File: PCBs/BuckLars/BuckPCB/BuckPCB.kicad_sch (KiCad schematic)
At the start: 8 parts, among them J1 Program_header, SW1 RESET, SW2 Boot, U1 ESP32-WROOM-32D

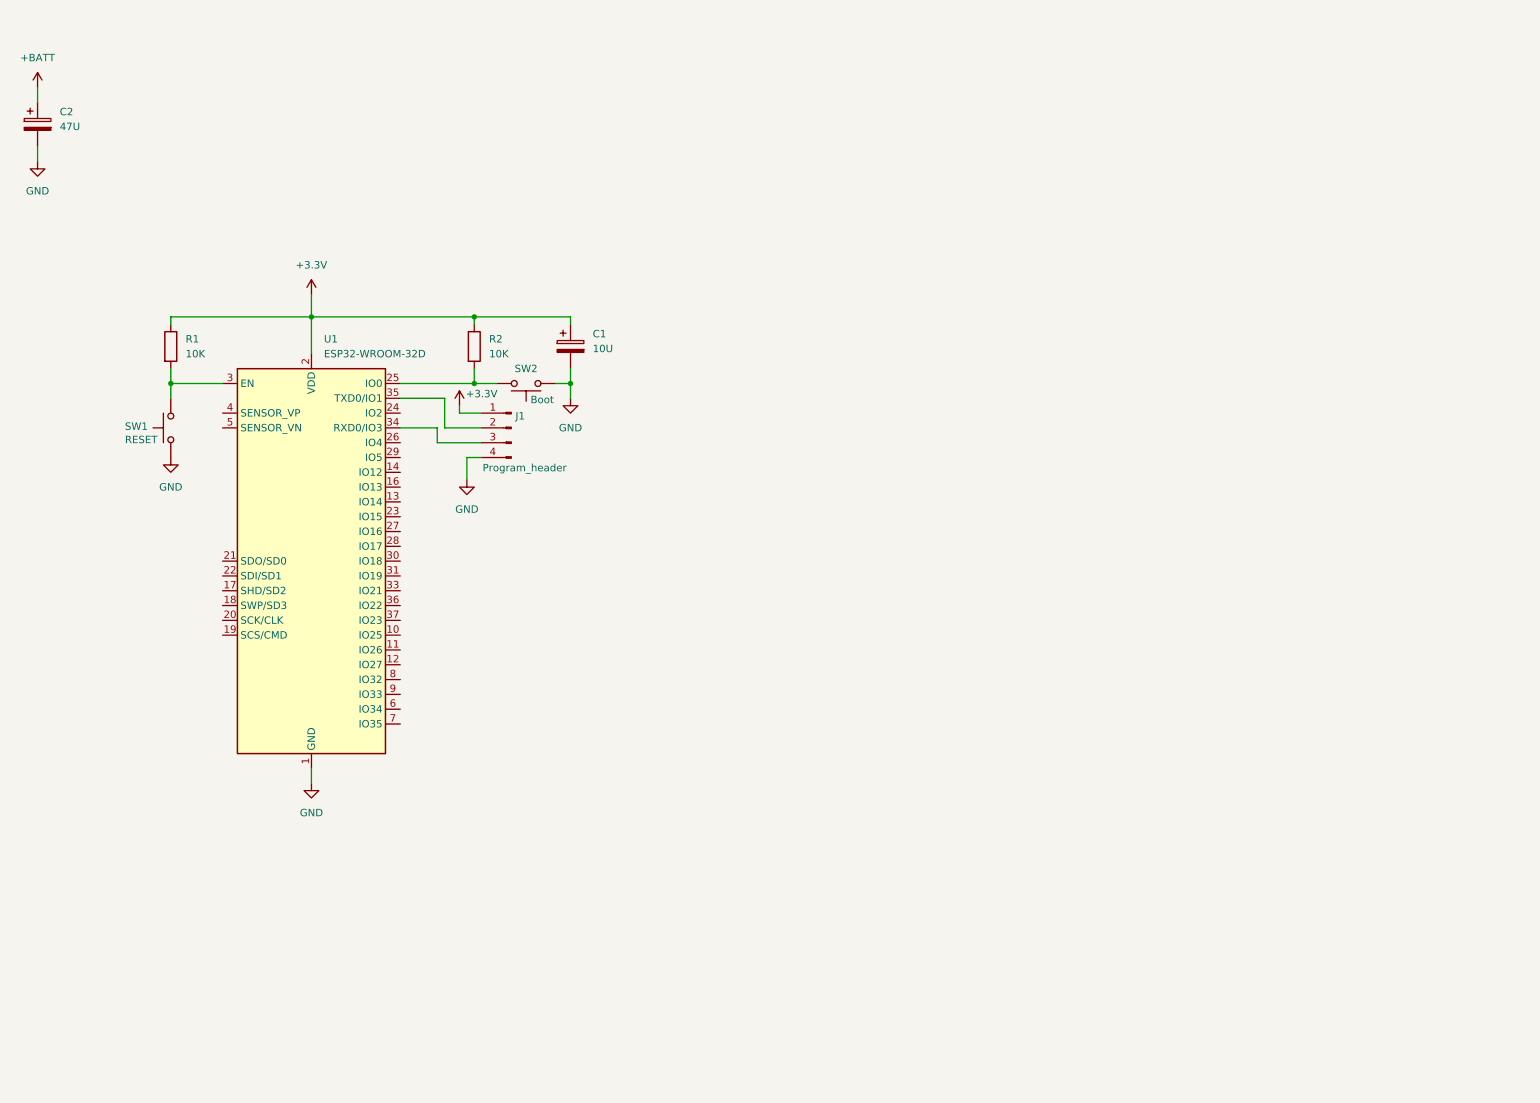
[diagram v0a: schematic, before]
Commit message: added buck converter to schematic
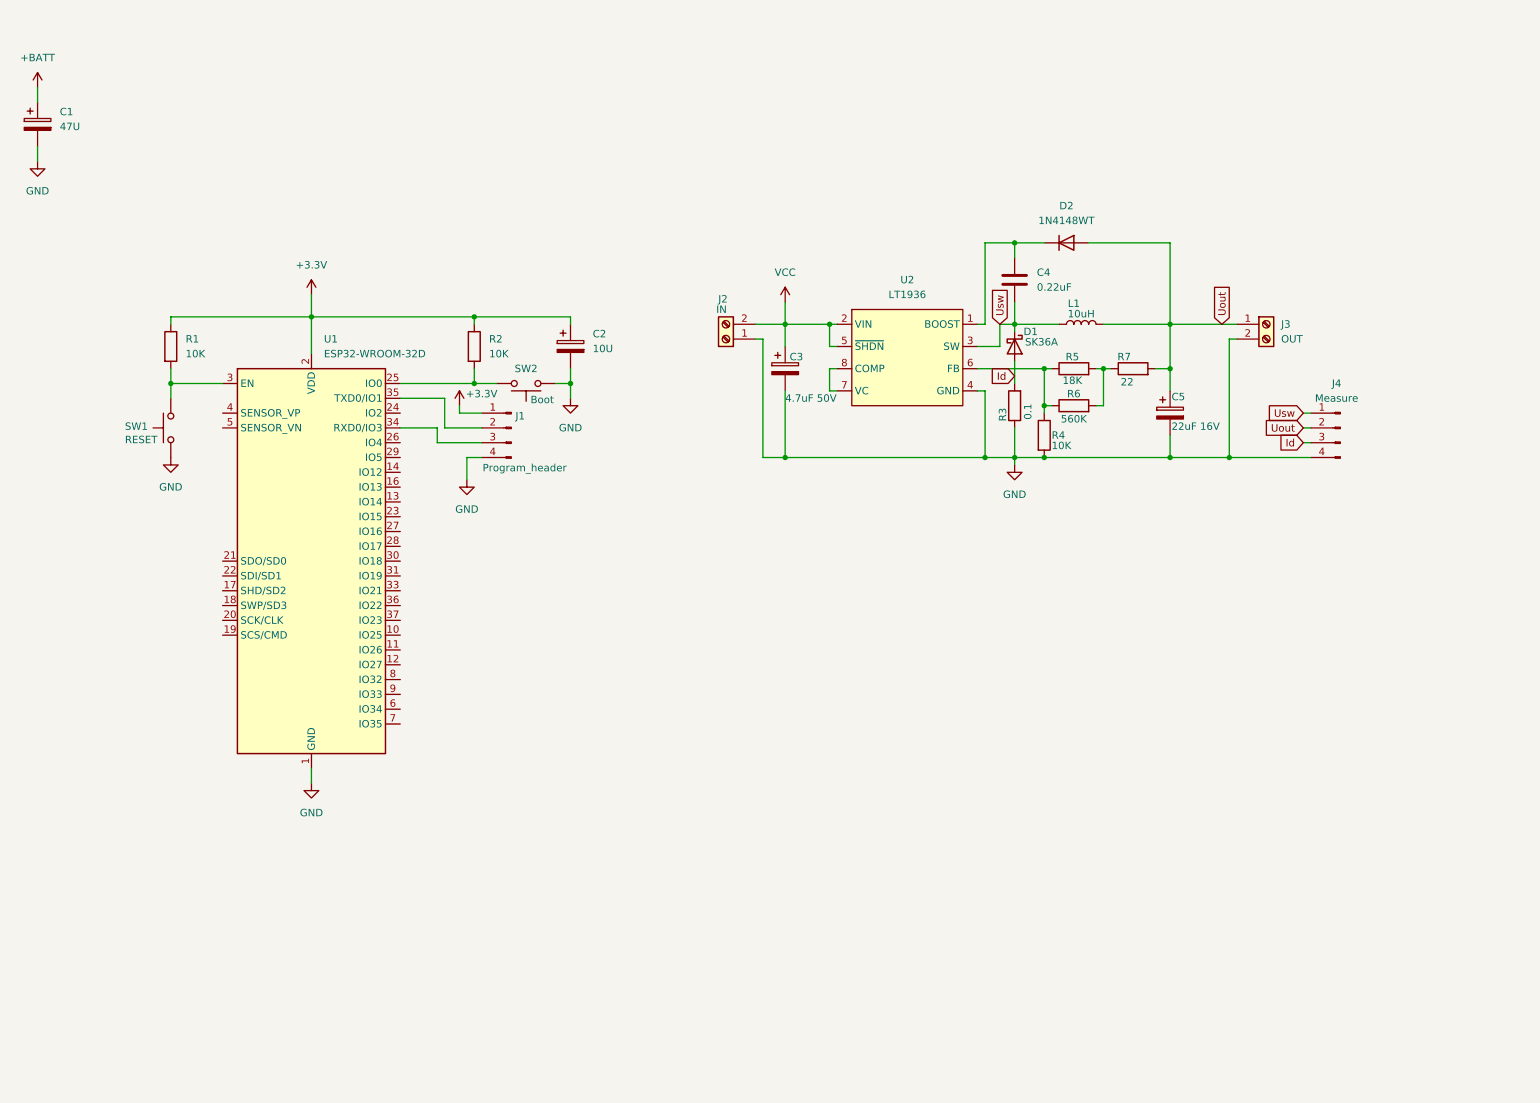
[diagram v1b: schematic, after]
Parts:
- added C3: 4.7uF 50V, Capacitor_SMD:CP_Elec_4x5.4, symbol Device:C_Polarized
- added C4: 0.22uF, Capacitor_SMD:C_1206_3216Metric_Pad1.33x1.80mm_HandSolder, symbol Device:C
- added C5: 22uF 16V, Capacitor_Tantalum_SMD:CP_EIA-3528-12_Kemet-T_HandSolder, symbol Device:C_Polarized
- added D1: SK36A, Diode_SMD:D_SMC, symbol Device:D_Schottky
- added D2: 1N4148WT, Diode_SMD:D_SOD-523, symbol Diode:1N4148WT
- added J2: IN, TerminalBlock:TerminalBlock_MaiXu_MX126-5.0-02P_1x02_P5.00mm, symbol Connector:Screw_Terminal_01x02
- added J3: OUT, TerminalBlock:TerminalBlock_MaiXu_MX126-5.0-02P_1x02_P5.00mm, symbol Connector:Screw_Terminal_01x02
- added J4: Measure, Connector_PinHeader_2.54mm:PinHeader_1x04_P2.54mm_Vertical, symbol Connector:Conn_01x04_Pin
- added L1: 10uH, Inductor_SMD:L_7.3x7.3_H4.5, symbol Device:L
- added R3: 0.1, Resistor_SMD:R_1206_3216Metric_Pad1.30x1.75mm_HandSolder, symbol Device:R
- added R4: 10K, Resistor_SMD:R_1206_3216Metric_Pad1.30x1.75mm_HandSolder, symbol Device:R
- added R5: 18K, Resistor_SMD:R_1206_3216Metric_Pad1.30x1.75mm_HandSolder, symbol Device:R
- added R6: 560K, Resistor_SMD:R_1206_3216Metric_Pad1.30x1.75mm_HandSolder, symbol Device:R
- added R7: 22, Resistor_SMD:R_1206_3216Metric_Pad1.30x1.75mm_HandSolder, symbol Device:R
- added U2: LT1936, Package_SO:MSOP-8-1EP_3x3mm_P0.65mm_EP1.95x2.15mm, symbol New_Library:LT1936
- renumbered C2 to C1, C1 to C2
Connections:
- net GND: now also C3.2, C5.2, J2.1 (Pin_1), J3.2 (Pin_2), J4.4 (Pin_4), R3.1, R4.2, U2.4 (GND)
- new net: R4.1, R5.1, R6.1, U2.6 (FB)
- new net: R5.2, R6.2, R7.1
- new net: C4.1, D2.1 (K), U2.1 (BOOST)
- new net: U2.7 (VC), U2.8 (COMP)
- new net Id: D1.2 (A), J4.3 (Pin_3), R3.2
- new net Uout: C5.1, D2.2 (A), J3.1 (Pin_1), J4.2 (Pin_2), L1.2, R7.2
- new net Usw: C4.2, D1.1 (K), J4.1 (Pin_1), L1.1, U2.3 (SW)
- new net VCC: C3.1, J2.2 (Pin_2), U2.2 (VIN), U2.5 (~{SHDN})

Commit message: cleanup chematic and assinged footprints
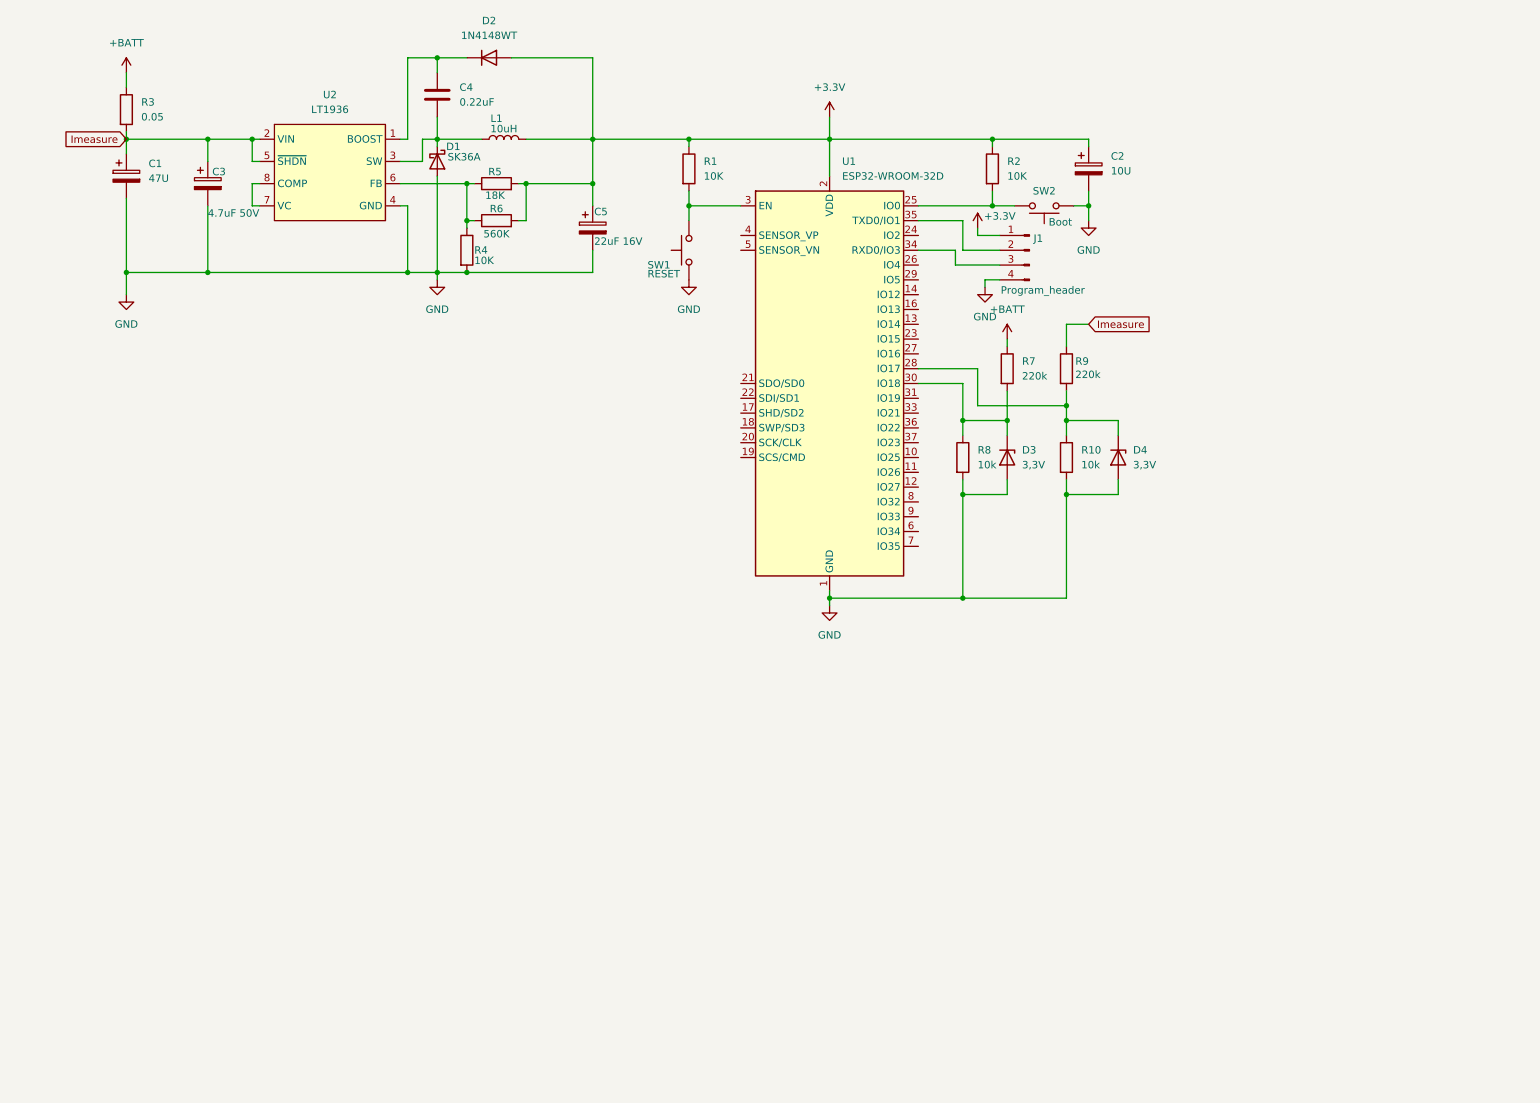
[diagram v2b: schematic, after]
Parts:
- removed J2: IN, TerminalBlock:TerminalBlock_MaiXu_MX126-5.0-02P_1x02_P5.00mm, symbol Connector:Screw_Terminal_01x02
- removed J3: OUT, TerminalBlock:TerminalBlock_MaiXu_MX126-5.0-02P_1x02_P5.00mm, symbol Connector:Screw_Terminal_01x02
- removed J4: Measure, Connector_PinHeader_2.54mm:PinHeader_1x04_P2.54mm_Vertical, symbol Connector:Conn_01x04_Pin
- added D3, D4: 3,3V, Diode_SMD:D_1206_3216Metric, symbol Device:D_Zener
- added R10, R8: 10k, Resistor_SMD:R_1206_3216Metric_Pad1.30x1.75mm_HandSolder, symbol Device:R
- added R9: 220k, Resistor_SMD:R_1206_3216Metric_Pad1.30x1.75mm_HandSolder, symbol Device:R
- C1, C2: footprint (none) -> Capacitor_SMD:CP_Elec_4x5.3
- J1: footprint (none) -> Connector_PinHeader_2.54mm:PinHeader_1x04_P2.54mm_Vertical
- R1, R2: footprint (none) -> Resistor_SMD:R_1206_3216Metric_Pad1.30x1.75mm_HandSolder
- R3: value 0.1 -> 0.05; footprint Resistor_SMD:R_1206_3216Metric_Pad1.30x1.75mm_HandSolder -> Resistor_SMD:R_4020_10251Metric_Pad1.65x5.30mm_HandSolder
- R7: value 22 -> 220k
- SW1, SW2: footprint (none) -> Button_Switch_SMD:SW_SPST_CK_RS282G05A3
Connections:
- net VCC is gone; now on net Imeasure: C3.1, U2.2 (VIN), U2.5 (~{SHDN})
- net +3.3V: now also C5.1, D2.2 (A), L1.2, R5.2, R6.2
- net +BATT: now also R3.1, R7.1; no longer C1.1
- net GND: now also D1.2 (A), D3.2 (A), D4.2 (A), R10.2, R8.2; no longer R3.1
- net at U1.28 (IO17): now also D4.1 (K), R10.1, R9.2
- net at U1.30 (IO18): now also R7.2, D3.1 (K), R8.1
- net Id renamed Imeasure
- net Imeasure: now also C1.1, R9.1; no longer D1.2 (A)
- removed net Uout: C5.1, D2.2 (A), L1.2, R7.2
- net Usw: no longer names the net of C4.2, D1.1 (K), L1.1, U2.3 (SW)
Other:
- moved on the sheet: C1, C2, C3, C4, C5, D1, D2, J1, L1, R1, R2, R4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

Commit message: added buck converters schematic
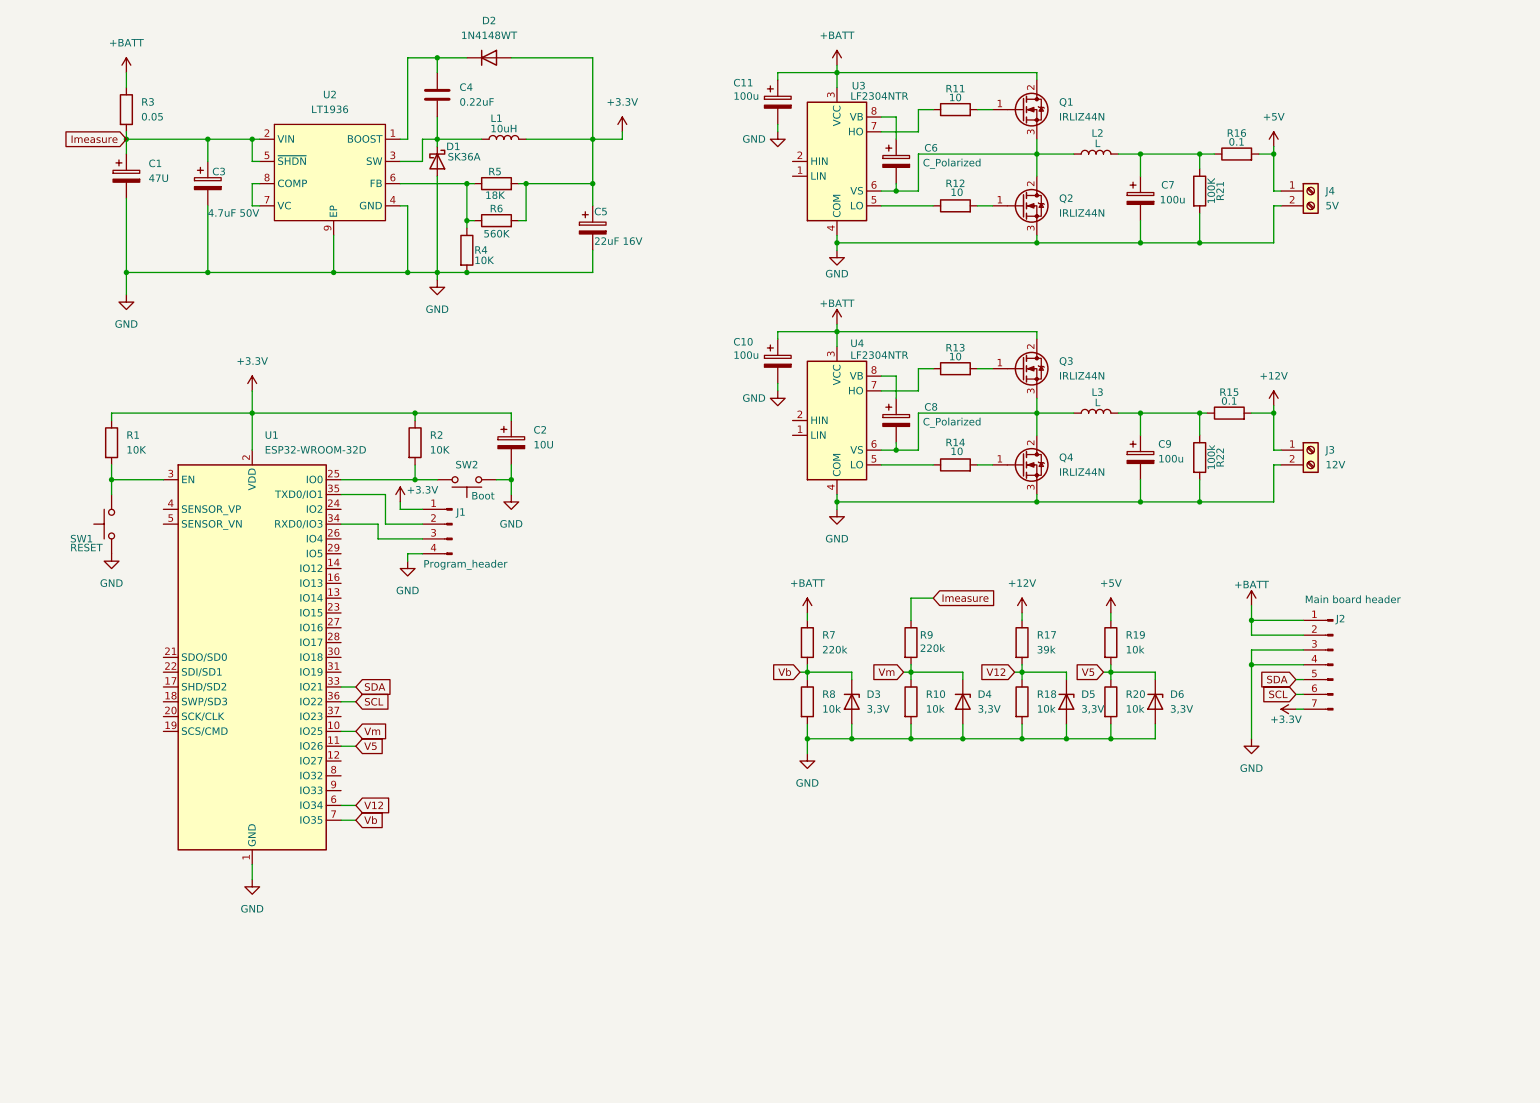
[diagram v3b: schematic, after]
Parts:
- added C10, C11, C7, C9: 100u, Capacitor_SMD:CP_Elec_8x10.5, symbol Device:C_Polarized
- added C6, C8: C_Polarized, Capacitor_SMD:CP_Elec_8x10.5, symbol Device:C_Polarized
- added D5, D6: 3,3V, Diode_SMD:D_1206_3216Metric, symbol Device:D_Zener
- added J2: Main board header, Connector_PinHeader_2.54mm:PinHeader_1x07_P2.54mm_Vertical, symbol Connector:Conn_01x07_Pin
- added J3: 12V, TerminalBlock:TerminalBlock_MaiXu_MX126-5.0-02P_1x02_P5.00mm, symbol Connector:Screw_Terminal_01x02
- added J4: 5V, TerminalBlock:TerminalBlock_MaiXu_MX126-5.0-02P_1x02_P5.00mm, symbol Connector:Screw_Terminal_01x02
- added L2, L3: L, Inductor_SMD:L_2512_6332Metric_Pad1.52x3.35mm_HandSolder, symbol Device:L
- added Q1, Q2, Q3, Q4: IRLIZ44N, Package_TO_SOT_THT:TO-220F-3_Vertical, symbol Transistor_FET:IRLIZ44N
- added R11, R12, R13, R14: 10, Resistor_SMD:R_1206_3216Metric_Pad1.30x1.75mm_HandSolder, symbol Device:R
- added R15, R16: 0.1, Resistor_SMD:R_1206_3216Metric_Pad1.30x1.75mm_HandSolder, symbol Device:R
- added R17: 39k, Resistor_SMD:R_1206_3216Metric_Pad1.30x1.75mm_HandSolder, symbol Device:R
- added R18, R19, R20: 10k, Resistor_SMD:R_1206_3216Metric_Pad1.30x1.75mm_HandSolder, symbol Device:R
- added R21: 100K, Resistor_SMD:R_1206_3216Metric_Pad1.30x1.75mm_HandSolder, symbol Device:R
- added R22: 100k, Resistor_SMD:R_1206_3216Metric_Pad1.30x1.75mm_HandSolder, symbol Device:R
- added U3, U4: LF2304NTR, Package_SO:SOIC-8_3.9x4.9mm_P1.27mm, symbol Driver_FET:IR2011
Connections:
- net +3.3V: now also J2.7 (Pin_7)
- net +BATT: now also C10.1, C11.1, J2.1 (Pin_1), J2.2 (Pin_2), Q1.2 (D), Q3.2 (D), U3.3 (VCC), U4.3 (VCC)
- net GND: now also U2.9 (EP), C10.2, C11.2, C7.2, C9.2, D5.2 (A), D6.2 (A), J2.3 (Pin_3), J2.4 (Pin_4), J3.2 (Pin_2), J4.2 (Pin_2), Q2.3 (S), Q4.3 (S), R18.2, R20.2, R21.2, R22.2, U3.4 (COM), U4.4 (COM)
- net Vm: now reaches U1.10 (IO25)
- net Vm: now also D4.1 (K), R10.1, R9.2
- net V5: now reaches U1.11 (IO26)
- net V5: now also D6.1 (K), R19.2, R20.1
- net Vb: now reaches D3.1 (K), R7.2, R8.1
- net Vb: now also U1.7 (IO35); no longer U1.30 (IO18)
- net SDA: now reaches U1.33 (IO21)
- net SDA: now also J2.5 (Pin_5)
- net SCL: now reaches U1.36 (IO22)
- net SCL: now also J2.6 (Pin_6)
- net V12: now reaches U1.6 (IO34)
- net V12: now also D5.1 (K), R17.2, R18.1
- new net: R14.1, U4.5 (LO)
- new net: C8.2, L3.1, Q3.3 (S), Q4.2 (D), U4.6 (VS)
- new net: R13.1, U4.7 (HO)
- new net: C8.1, U4.8 (VB)
- new net: C6.2, L2.1, Q1.3 (S), Q2.2 (D), U3.6 (VS)
- new net: C7.1, L2.2, R16.1, R21.1
- new net: C6.1, U3.8 (VB)
- new net: Q4.1 (G), R14.2
- new net: Q3.1 (G), R13.2
- new net: C9.1, L3.2, R15.1, R22.1
- new net: Q2.1 (G), R12.2
- new net: Q1.1 (G), R11.2
- new net: R12.1, U3.5 (LO)
- new net: R11.1, U3.7 (HO)
- new net +12V: J3.1 (Pin_1), R15.2, R17.1
- new net +5V: J4.1 (Pin_1), R16.2, R19.1
- now unconnected: U1.28 (IO17)
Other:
- moved on the sheet: C2, D3, D4, J1, R1, R10, R2, R7, R8, R9, SW1, SW2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
